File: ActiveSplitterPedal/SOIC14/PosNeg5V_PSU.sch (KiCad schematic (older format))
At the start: 12 parts, among them U3 TPS60400, U9 SE8250X2

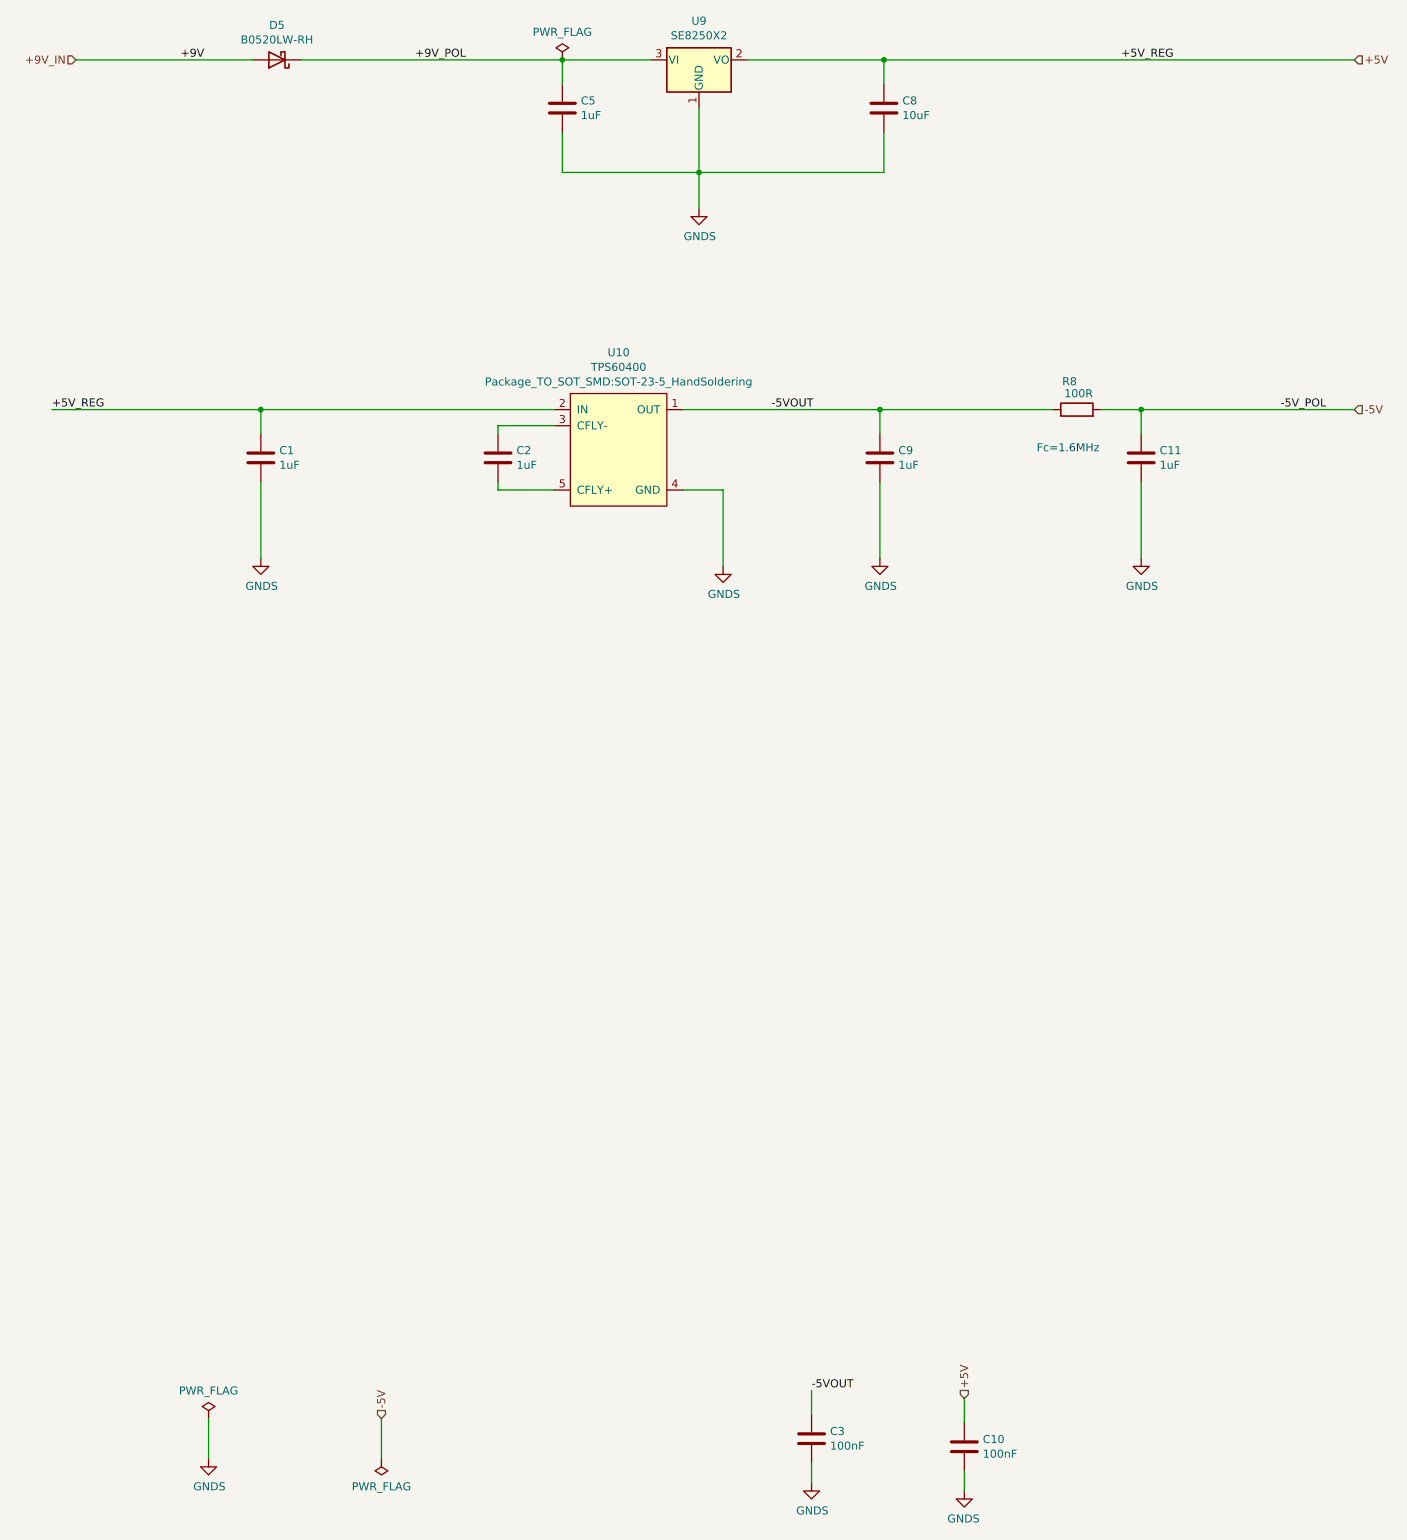
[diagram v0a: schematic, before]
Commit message: RevA HW updates
- Replaced SW Diode with Schottky Diode
- Added one charge pump IC per quad opamp (60mA each)
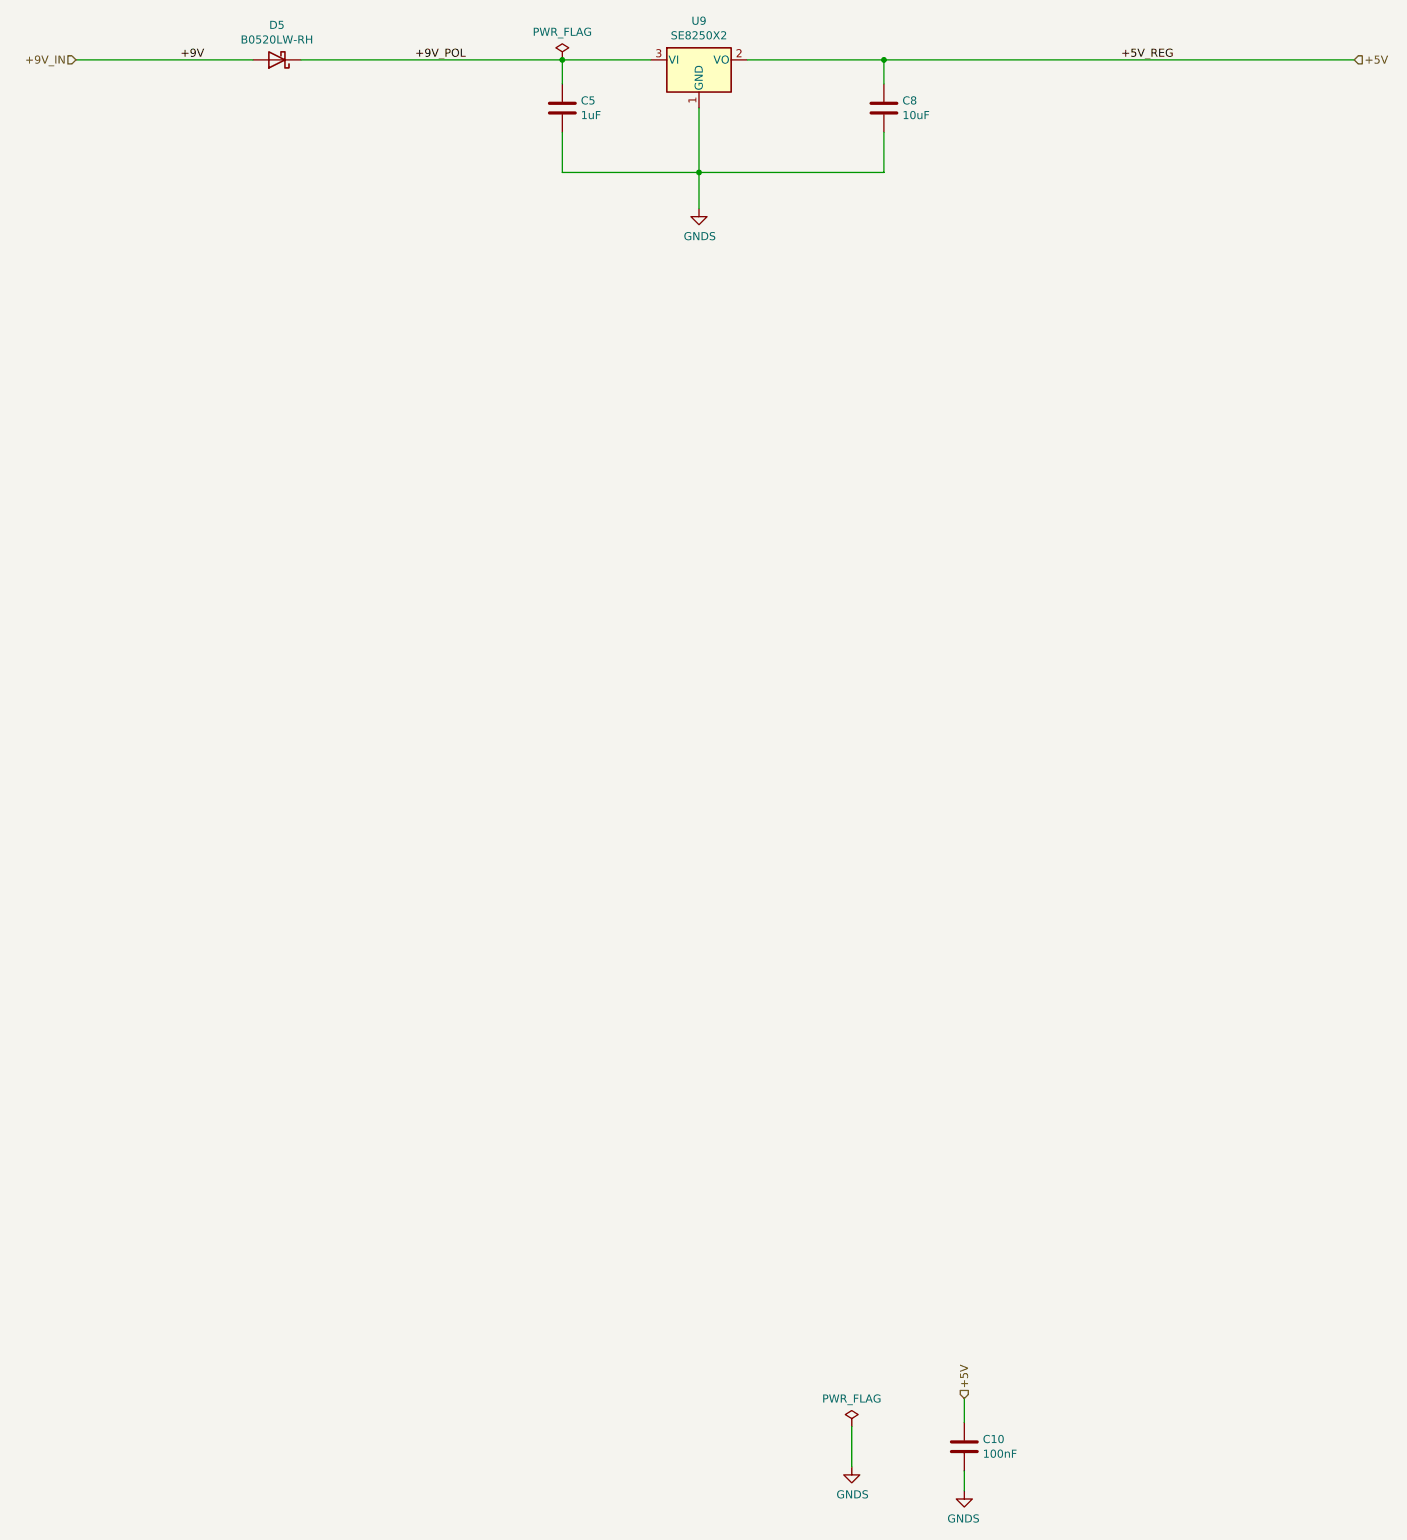
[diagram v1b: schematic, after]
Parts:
- removed C13, C3, C4, C5: 1uF, Capacitor_SMD:C_0805_2012Metric_Pad1.15x1.40mm_HandSolder, symbol Device:C
- removed C7: 100nF, Capacitor_SMD:C_0805_2012Metric_Pad1.15x1.40mm_HandSolder, symbol Device:C
- removed R7: 100R, Resistor_SMD:R_0805_2012Metric_Pad1.15x1.40mm_HandSolder, symbol Device:R
- removed U3: TPS60400, Package_TO_SOT_SMD:SOT-23-5_HandSoldering, symbol TPS6040x:TPS60400
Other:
- note removed: "Fc=1.6MHz"

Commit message: added uv etch layout
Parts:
- D5: footprint Diode_SMD:D_SMB_Handsoldering -> Diode_SMD:D_SOD-123F
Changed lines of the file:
@@
 F 0 "D5" H 5025 1459 50  0000 C CNN
 F 1 "B0520LW-RH" H 5025 1550 50  0000 C CNN
-F 2 "Diode_SMD:D_SMB_Handsoldering" H 5025 1675 50  0001 C CNN
+F 2 "Diode_SMD:D_SOD-123F" H 5025 1675 50  0001 C CNN
 F 3 "https://www.taiwansemi.com/products/datasheet/B0520LW%20SERIES_I1601.pdf" H 5025 1675 50  0001 C CNN
 	1    5025 1675
